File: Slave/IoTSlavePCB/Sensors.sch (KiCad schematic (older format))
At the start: 0 parts

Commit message: Continued work on slaves. Added sensor and begun work on ZigBee transceiver.
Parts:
- added C?: 100 nF, Capacitor_SMD:C_0603_1608Metric, symbol Device:C
- added R? (x2): 10k, Resistor_SMD:R_0603_1608Metric, symbol Device:R
- added U?: SHTC3, Personal_ICs:SHTC3, symbol Personal_ICs:SHTC3
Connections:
- new net +1V8: C?.2, R?.1, R?.1, U?.1 (VDD)
- new net GND: C?.1, U?.4 (VSS), U?.5 (PAD)
- new net SCL: R?.2, U?.2 (SCL)
- new net SDA: R?.2, U?.3 (SDA)
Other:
- note added: "Temperature and humidity sensor"
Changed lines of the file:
@@
 $Descr A4 11693 8268
 encoding utf-8
-Sheet 1 5
+Sheet 4 5
 Title "IoT Slave Board"
 Date "2020-11-01"
@@
 Comment4 ""
 $EndDescr
+$Comp
+L Personal_ICs:SHTC3 U?
+U 1 1 5FA55026
+P 1700 1700
+F 0 "U?" H 2200 1350 50  0000 C CNN
+F 1 "SHTC3" H 2200 1250 50  0000 C CNN
+F 2 "Personal_ICs:SHTC3" H 2550 1800 50  0001 L CNN
+F 3 "https://www.glynshop.com/erp/owweb/Daten/Datenblaetter/Sensirion/SHTC3.pdf" H 2550 1700 50  0001 L CNN
+F 4 "Humidity and Temperature Sensor IC" H 2550 1600 50  0001 L CNN "Description"
+F 5 "0.75" H 2550 1500 50  0001 L CNN "Height"
+F 6 "Sensirion" H 2550 1400 50  0001 L CNN "Manufacturer_Name"
+F 7 "SHTC3" H 2550 1300 50  0001 L CNN "Manufacturer_Part_Number"
+F 8 "SHTC3" H 2550 1200 50  0001 L CNN "Arrow Part Number"
+F 9 "https://www.arrow.com/en/products/shtc3/sensirion-ag" H 2550 1100 50  0001 L CNN "Arrow Price/Stock"
+F 10 "403-SHTC3" H 2550 1000 50  0001 L CNN "Mouser Part Number"
+F 11 "https://www.mouser.co.uk/ProductDetail/Sensirion/SHTC3?qs=y6ZabgHbY%252Bx3LlA87fqBwg%3D%3D" H 2550 900 50  0001 L CNN "Mouser Price/Stock"
+	1    1700 1700
+	1    0    0    -1
+$EndComp
+$Comp
+L power:+1V8 #PWR?
+U 1 1 5FA567F3
+P 1700 1300
+F 0 "#PWR?" H 1700 1150 50  0001 C CNN
+F 1 "+1V8" H 1700 1450 50  0000 C CNN
+F 2 "" H 1700 1300 50  0001 C CNN
+F 3 "" H 1700 1300 50  0001 C CNN
+	1    1700 1300
+	1    0    0    -1
+$EndComp
+$Comp
+L Device:C C?
+U 1 1 5FA57F6A
+P 2200 1300
+F 0 "C?" V 1948 1300 50  0000 C CNN
+F 1 "100 nF" V 2039 1300 50  0000 C CNN
+F 2 "Capacitor_SMD:C_0603_1608Metric" H 2238 1150 50  0001 C CNN
+F 3 "~" H 2200 1300 50  0001 C CNN
+	1    2200 1300
+	0    1    1    0
+$EndComp
+Wire Wire Line
+	2350 1300 2700 1300
+Wire Wire Line
+	2700 1300 2700 1700
+Wire Wire Line
+	2050 1300 1700 1300
+Wire Wire Line
+	1700 1300 1700 1700
+Connection ~ 1700 1300
+$Comp
+L power:GND #PWR?
+U 1 1 5FA5943C
+P 2700 1300
+F 0 "#PWR?" H 2700 1050 50  0001 C CNN
+F 1 "GND" H 2700 1150 50  0000 C CNN
+F 2 "" H 2700 1300 50  0001 C CNN
+F 3 "" H 2700 1300 50  0001 C CNN
+	1    2700 1300
+	-1   0    0    1
+$EndComp
+Connection ~ 2700 1300
+Wire Wire Line
+	2700 1800 2700 1700
+Connection ~ 2700 1700
+$Comp
+L Device:R R?
+U 1 1 5FA5AF56
+P 1450 1550
+F 0 "R?" H 1500 1600 50  0000 L CNN
+F 1 "10k" H 1500 1500 50  0000 L CNN
+F 2 "Resistor_SMD:R_0603_1608Metric" V 1380 1550 50  0001 C CNN
+F 3 "~" H 1450 1550 50  0001 C CNN
+	1    1450 1550
+	1    0    0    -1
+$EndComp
+$Comp
+L Device:R R?
+U 1 1 5FA5B59C
+P 1350 1550
+F 0 "R?" H 1200 1600 50  0000 L CNN
+F 1 "10k" H 1150 1500 50  0000 L CNN
+F 2 "Resistor_SMD:R_0603_1608Metric" V 1280 1550 50  0001 C CNN
+F 3 "~" H 1350 1550 50  0001 C CNN
+	1    1350 1550
+	1    0    0    -1
+$EndComp
+Wire Wire Line
+	1250 1800 1350 1800
+Wire Wire Line
+	1250 1900 1450 1900
+Wire Wire Line
+	1450 1900 1450 1700
+Connection ~ 1450 1900
+Wire Wire Line
+	1450 1900 1700 1900
+Wire Wire Line
+	1350 1800 1350 1700
+Connection ~ 1350 1800
+Wire Wire Line
+	1350 1800 1700 1800
+Wire Wire Line
+	1450 1400 1450 1300
+Wire Wire Line
+	1450 1300 1700 1300
+Wire Wire Line
+	1350 1400 1350 1300
+Wire Wire Line
+	1350 1300 1450 1300
+Connection ~ 1450 1300
+Text HLabel 1250 1800 0    50   Input ~ 0
+SCL
+Text HLabel 1250 1900 0    50   BiDi ~ 0
+SDA
+Wire Notes Line
+	950  2200 950  1000
+Wire Notes Line
+	950  1000 2850 1000
+Wire Notes Line
+	2850 1000 2850 2200
+Wire Notes Line
+	2850 2200 950  2200
+Text Notes 950  1000 0    50   ~ 0
+Temperature and humidity sensor
 $EndSCHEMATC

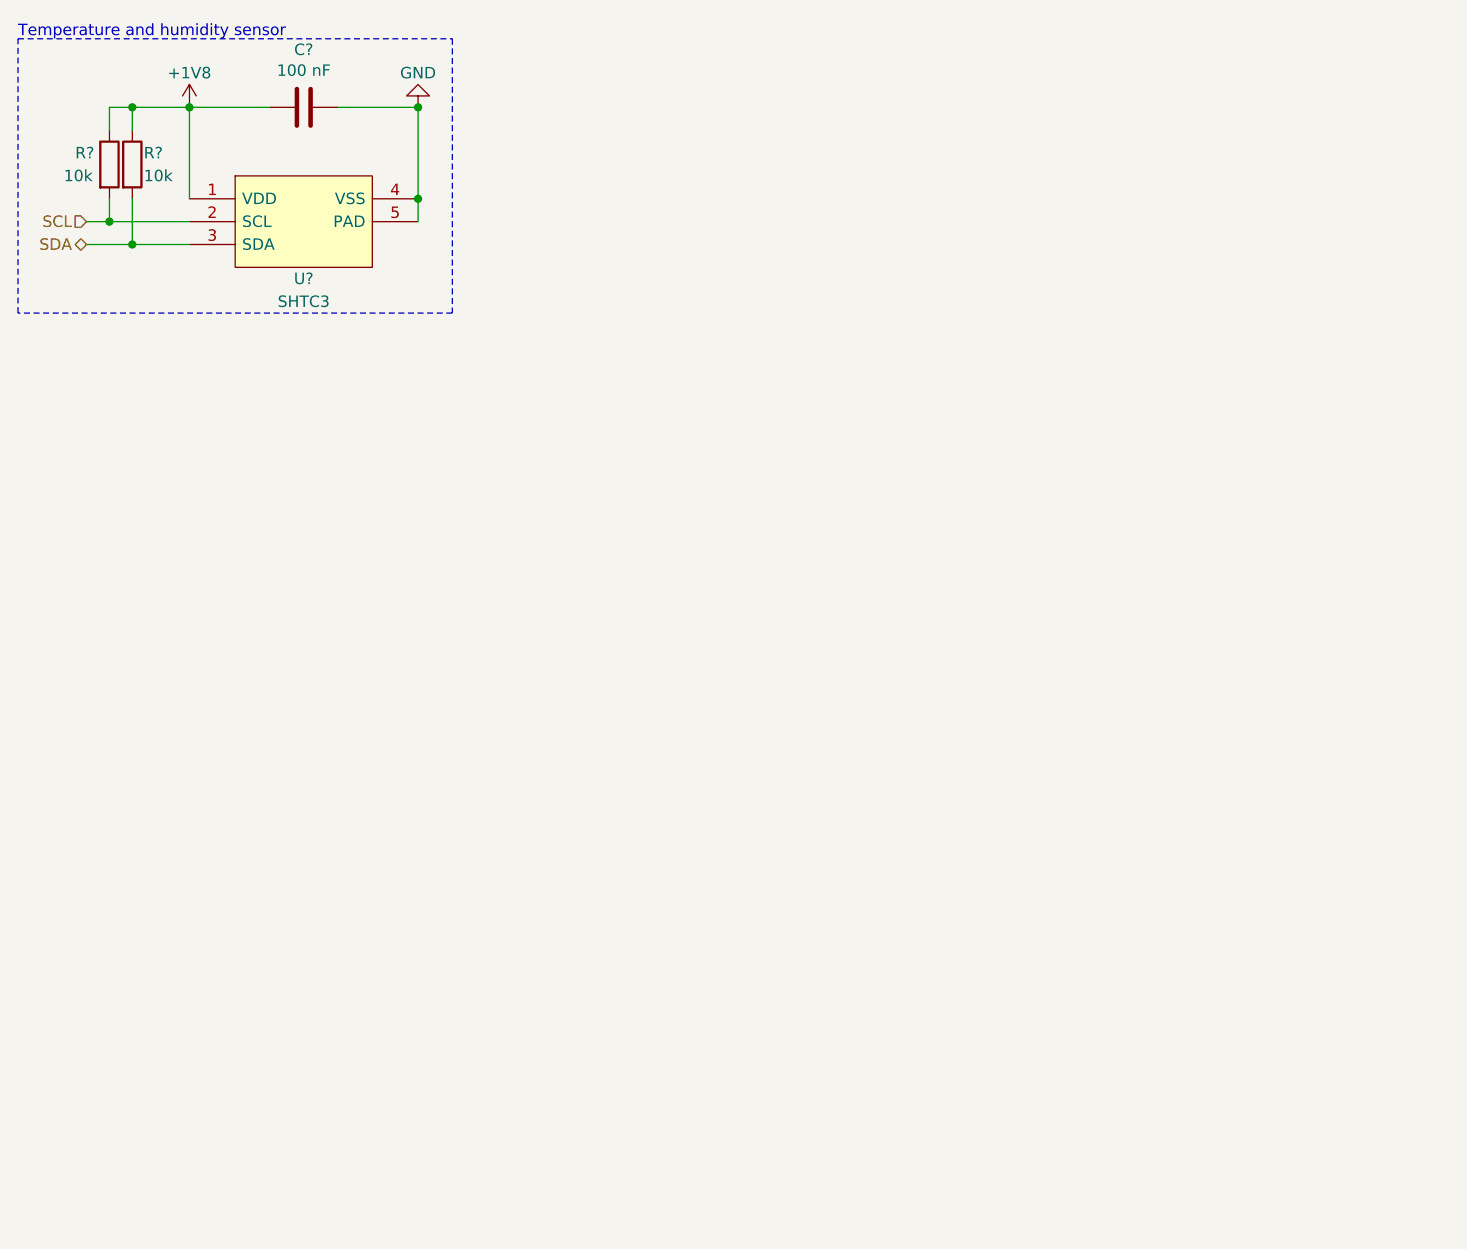
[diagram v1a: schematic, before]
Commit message: Finished slave schematics, including memory and Zigbee Transceiver. Further work on PCB, well underway.
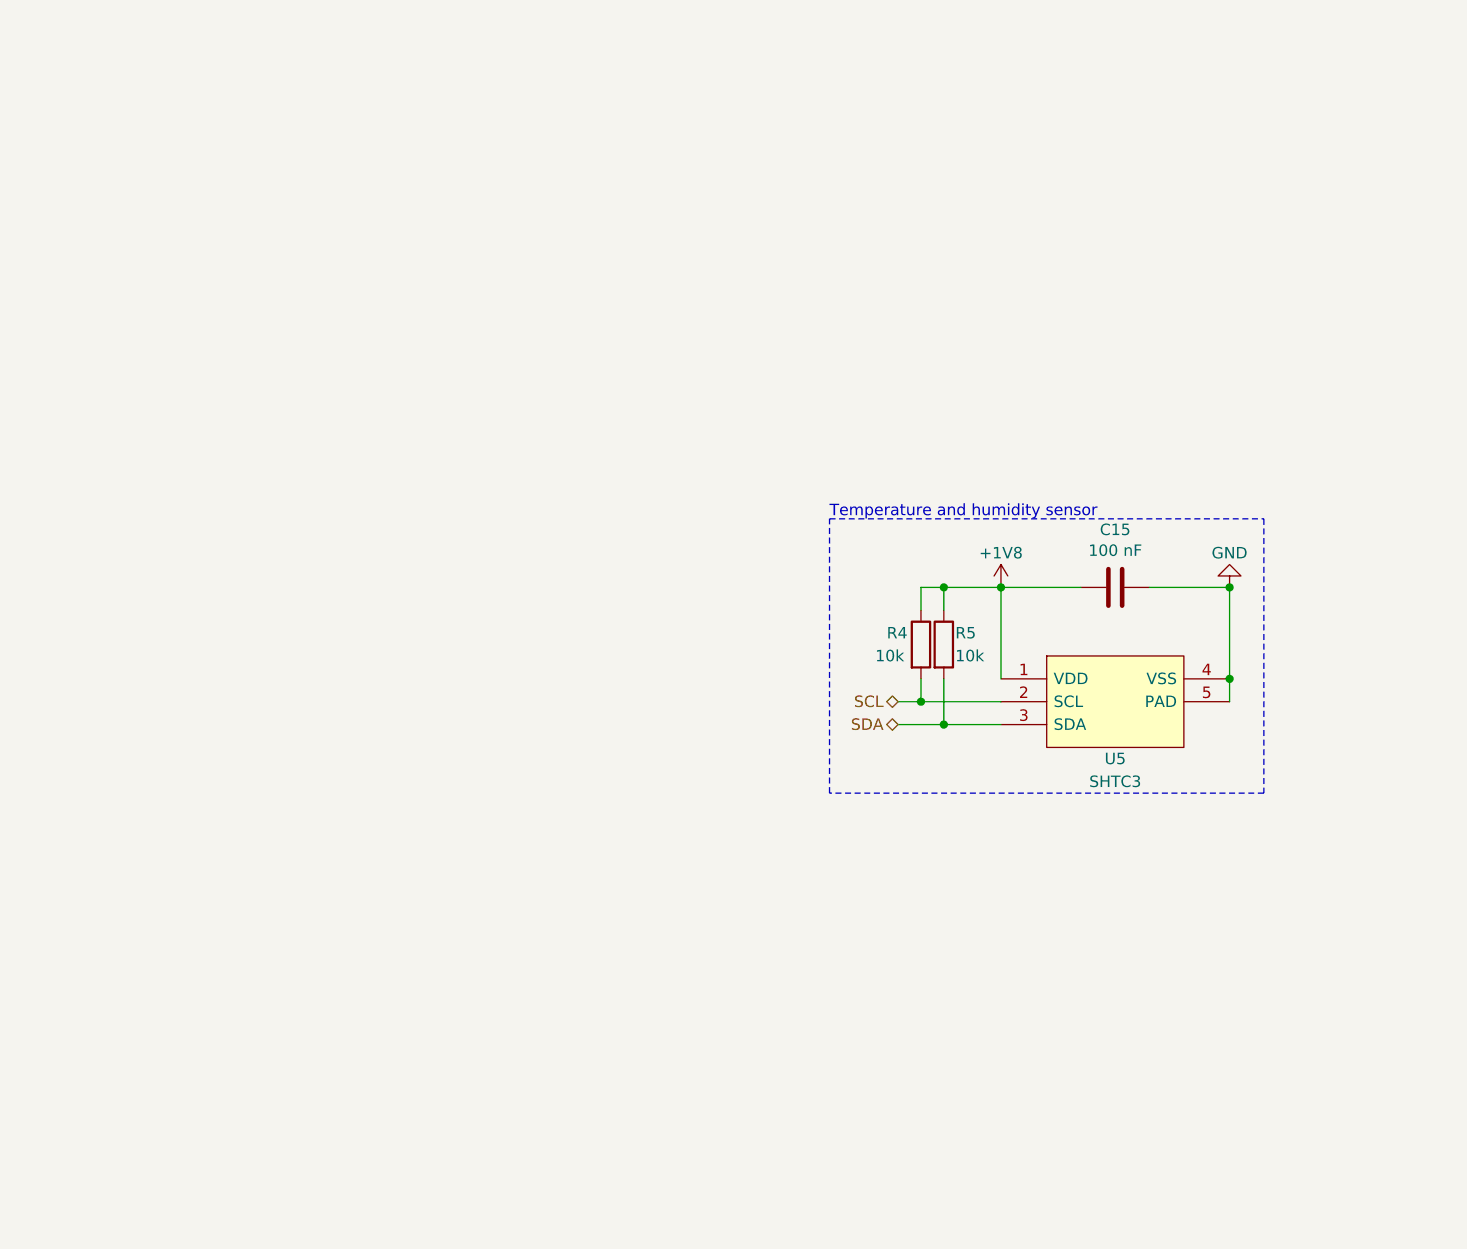
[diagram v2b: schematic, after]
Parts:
- gave numbers to parts that had none: 4
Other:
- moved on the sheet: C15, R4, R5, U5
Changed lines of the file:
@@
 $Descr A4 11693 8268
 encoding utf-8
-Sheet 4 5
+Sheet 4 6
 Title "IoT Slave Board"
 Date "2020-11-01"
@@
 $EndDescr
 $Comp
-L Personal_ICs:SHTC3 U?
+L Personal_ICs:SHTC3 U5
 U 1 1 5FA55026
-P 1700 1700
-F 0 "U?" H 2200 1350 50  0000 C CNN
-F 1 "SHTC3" H 2200 1250 50  0000 C CNN
-F 2 "Personal_ICs:SHTC3" H 2550 1800 50  0001 L CNN
-F 3 "https://www.glynshop.com/erp/owweb/Daten/Datenblaetter/Sensirion/SHTC3.pdf" H 2550 1700 50  0001 L CNN
-F 4 "Humidity and Temperature Sensor IC" H 2550 1600 50  0001 L CNN "Description"
-F 5 "0.75" H 2550 1500 50  0001 L CNN "Height"
-F 6 "Sensirion" H 2550 1400 50  0001 L CNN "Manufacturer_Name"
-F 7 "SHTC3" H 2550 1300 50  0001 L CNN "Manufacturer_Part_Number"
-F 8 "SHTC3" H 2550 1200 50  0001 L CNN "Arrow Part Number"
-F 9 "https://www.arrow.com/en/products/shtc3/sensirion-ag" H 2550 1100 50  0001 L CNN "Arrow Price/Stock"
-F 10 "403-SHTC3" H 2550 1000 50  0001 L CNN "Mouser Part Number"
-F 11 "https://www.mouser.co.uk/ProductDetail/Sensirion/SHTC3?qs=y6ZabgHbY%252Bx3LlA87fqBwg%3D%3D" H 2550 900 50  0001 L CNN "Mouser Price/Stock"
-	1    1700 1700
+P 5250 3800
+F 0 "U5" H 5750 3450 50  0000 C CNN
+F 1 "SHTC3" H 5750 3350 50  0000 C CNN
+F 2 "Personal_ICs:SHTC3" H 6100 3900 50  0001 L CNN
+F 3 "https://www.glynshop.com/erp/owweb/Daten/Datenblaetter/Sensirion/SHTC3.pdf" H 6100 3800 50  0001 L CNN
+F 4 "Humidity and Temperature Sensor IC" H 6100 3700 50  0001 L CNN "Description"
+F 5 "0.75" H 6100 3600 50  0001 L CNN "Height"
+F 6 "Sensirion" H 6100 3500 50  0001 L CNN "Manufacturer_Name"
+F 7 "SHTC3" H 6100 3400 50  0001 L CNN "Manufacturer_Part_Number"
+F 8 "SHTC3" H 6100 3300 50  0001 L CNN "Arrow Part Number"
+F 9 "https://www.arrow.com/en/products/shtc3/sensirion-ag" H 6100 3200 50  0001 L CNN "Arrow Price/Stock"
+F 10 "403-SHTC3" H 6100 3100 50  0001 L CNN "Mouser Part Number"
+F 11 "https://www.mouser.co.uk/ProductDetail/Sensirion/SHTC3?qs=y6ZabgHbY%252Bx3LlA87fqBwg%3D%3D" H 6100 3000 50  0001 L CNN "Mouser Price/Stock"
+	1    5250 3800
 	1    0    0    -1
 $EndComp
 $Comp
-L power:+1V8 #PWR?
+L power:+1V8 #PWR044
 U 1 1 5FA567F3
-P 1700 1300
-F 0 "#PWR?" H 1700 1150 50  0001 C CNN
-F 1 "+1V8" H 1700 1450 50  0000 C CNN
-F 2 "" H 1700 1300 50  0001 C CNN
-F 3 "" H 1700 1300 50  0001 C CNN
-	1    1700 1300
+P 5250 3400
+F 0 "#PWR044" H 5250 3250 50  0001 C CNN
+F 1 "+1V8" H 5250 3550 50  0000 C CNN
+F 2 "" H 5250 3400 50  0001 C CNN
+F 3 "" H 5250 3400 50  0001 C CNN
+	1    5250 3400
 	1    0    0    -1
 $EndComp
 $Comp
-L Device:C C?
+L Device:C C15
 U 1 1 5FA57F6A
-P 2200 1300
-F 0 "C?" V 1948 1300 50  0000 C CNN
-F 1 "100 nF" V 2039 1300 50  0000 C CNN
-F 2 "Capacitor_SMD:C_0603_1608Metric" H 2238 1150 50  0001 C CNN
-F 3 "~" H 2200 1300 50  0001 C CNN
-	1    2200 1300
+P 5750 3400
+F 0 "C15" V 5498 3400 50  0000 C CNN
+F 1 "100 nF" V 5589 3400 50  0000 C CNN
+F 2 "Capacitor_SMD:C_0603_1608Metric" H 5788 3250 50  0001 C CNN
+F 3 "~" H 5750 3400 50  0001 C CNN
+	1    5750 3400
 	0    1    1    0
 $EndComp
 Wire Wire Line
-	2350 1300 2700 1300
+	5900 3400 6250 3400
 Wire Wire Line
-	2700 1300 2700 1700
+	6250 3400 6250 3800
 Wire Wire Line
-	2050 1300 1700 1300
+	5600 3400 5250 3400
 Wire Wire Line
-	1700 1300 1700 1700
-Connection ~ 1700 1300
+	5250 3400 5250 3800
+Connection ~ 5250 3400
 $Comp
-L power:GND #PWR?
+L power:GND #PWR045
 U 1 1 5FA5943C
-P 2700 1300
-F 0 "#PWR?" H 2700 1050 50  0001 C CNN
-F 1 "GND" H 2700 1150 50  0000 C CNN
-F 2 "" H 2700 1300 50  0001 C CNN
-F 3 "" H 2700 1300 50  0001 C CNN
-	1    2700 1300
+P 6250 3400
+F 0 "#PWR045" H 6250 3150 50  0001 C CNN
+F 1 "GND" H 6250 3250 50  0000 C CNN
+F 2 "" H 6250 3400 50  0001 C CNN
+F 3 "" H 6250 3400 50  0001 C CNN
+	1    6250 3400
 	-1   0    0    1
 $EndComp
-Connection ~ 2700 1300
+Connection ~ 6250 3400
 Wire Wire Line
-	2700 1800 2700 1700
-Connection ~ 2700 1700
+	6250 3900 6250 3800
+Connection ~ 6250 3800
 $Comp
-L Device:R R?
+L Device:R R5
 U 1 1 5FA5AF56
-P 1450 1550
-F 0 "R?" H 1500 1600 50  0000 L CNN
-F 1 "10k" H 1500 1500 50  0000 L CNN
-F 2 "Resistor_SMD:R_0603_1608Metric" V 1380 1550 50  0001 C CNN
-F 3 "~" H 1450 1550 50  0001 C CNN
-	1    1450 1550
+P 5000 3650
+F 0 "R5" H 5050 3700 50  0000 L CNN
+F 1 "10k" H 5050 3600 50  0000 L CNN
+F 2 "Resistor_SMD:R_0603_1608Metric" V 4930 3650 50  0001 C CNN
+F 3 "~" H 5000 3650 50  0001 C CNN
+	1    5000 3650
 	1    0    0    -1
 $EndComp
 $Comp
-L Device:R R?
+L Device:R R4
 U 1 1 5FA5B59C
-P 1350 1550
-F 0 "R?" H 1200 1600 50  0000 L CNN
-F 1 "10k" H 1150 1500 50  0000 L CNN
-F 2 "Resistor_SMD:R_0603_1608Metric" V 1280 1550 50  0001 C CNN
-F 3 "~" H 1350 1550 50  0001 C CNN
-	1    1350 1550
+P 4900 3650
+F 0 "R4" H 4750 3700 50  0000 L CNN
+F 1 "10k" H 4700 3600 50  0000 L CNN
+F 2 "Resistor_SMD:R_0603_1608Metric" V 4830 3650 50  0001 C CNN
+F 3 "~" H 4900 3650 50  0001 C CNN
+	1    4900 3650
 	1    0    0    -1
 $EndComp
 Wire Wire Line
-	1250 1800 1350 1800
+	4800 3900 4900 3900
 Wire Wire Line
-	1250 1900 1450 1900
+	4800 4000 5000 4000
 Wire Wire Line
-	1450 1900 1450 1700
-Connection ~ 1450 1900
+	5000 4000 5000 3800
+Connection ~ 5000 4000
 Wire Wire Line
-	1450 1900 1700 1900
+	5000 4000 5250 4000
 Wire Wire Line
-	1350 1800 1350 1700
-Connection ~ 1350 1800
+	4900 3900 4900 3800
+Connection ~ 4900 3900
 Wire Wire Line
-	1350 1800 1700 1800
+	4900 3900 5250 3900
 Wire Wire Line
-	1450 1400 1450 1300
+	5000 3500 5000 3400
 Wire Wire Line
-	1450 1300 1700 1300
+	5000 3400 5250 3400
 Wire Wire Line
-	1350 1400 1350 1300
+	4900 3500 4900 3400
 Wire Wire Line
-	1350 1300 1450 1300
-Connection ~ 1450 1300
-Text HLabel 1250 1800 0    50   Input ~ 0
+	4900 3400 5000 3400
+Connection ~ 5000 3400
+Text HLabel 4800 3900 0    50   BiDi ~ 0
 SCL
-Text HLabel 1250 1900 0    50   BiDi ~ 0
+Text HLabel 4800 4000 0    50   BiDi ~ 0
 SDA
 Wire Notes Line
-	950  2200 950  1000
+	4500 4300 4500 3100
 Wire Notes Line
-	950  1000 2850 1000
+	4500 3100 6400 3100
 Wire Notes Line
-	2850 1000 2850 2200
+	6400 3100 6400 4300
 Wire Notes Line
-	2850 2200 950  2200
-Text Notes 950  1000 0    50   ~ 0
+	6400 4300 4500 4300
+Text Notes 4500 3100 0    50   ~ 0
 Temperature and humidity sensor
 $EndSCHEMATC
